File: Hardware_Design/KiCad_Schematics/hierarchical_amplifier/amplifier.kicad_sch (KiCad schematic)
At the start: 8 parts, among them Q1 BC547

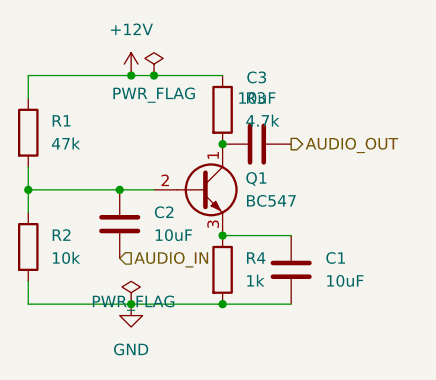
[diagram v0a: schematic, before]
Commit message: Add README for Hierarchical Amplifier circuit
Added the README.md file for the Hierarchical Amplifier project. This file includes the project purpose, component details, functional explanation of the circuit elements (voltage divider, coupling/bypass capacitors), and schematic references to support the hierarchical design documentation.
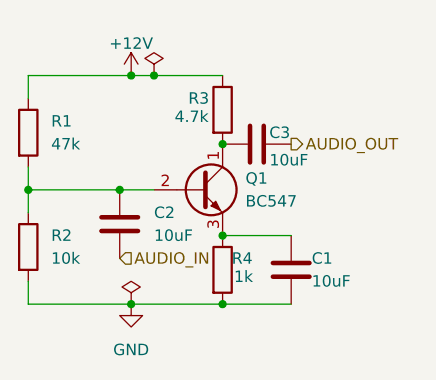
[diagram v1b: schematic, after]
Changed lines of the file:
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@@
 		)
 		(instances
-			(project "kurs4"
+			(project "hierarchical_amplifier"
 				(path "/1680d475-8d12-44de-9d5b-0889d33728e7/cbe5c0ee-a82d-4d0f-91ce-87dab7d0ab98"
 					(reference "#PWR03")
@@
 		(in_pos_files yes)
 		(dnp no)
-		(fields_autoplaced yes)
 		(property "Reference" "#PWR01"
 			(at 133.35 90.17 0)
@@
 		)
 		(property "Value" "+12V"
-			(at 133.35 81.28 0)
+			(at 133.35 82.804 0)
 			(show_name no)
 			(do_not_autoplace no)
@@
 		)
 		(instances
-			(project "kurs4"
+			(project "hierarchical_amplifier"
 				(path "/1680d475-8d12-44de-9d5b-0889d33728e7/cbe5c0ee-a82d-4d0f-91ce-87dab7d0ab98"
 					(reference "#PWR01")
@@
 		)
 		(instances
-			(project "kurs4"
+			(project "hierarchical_amplifier"
 				(path "/1680d475-8d12-44de-9d5b-0889d33728e7/cbe5c0ee-a82d-4d0f-91ce-87dab7d0ab98"
 					(reference "Q1")
@@
 		)
 		(instances
-			(project "kurs4"
+			(project "hierarchical_amplifier"
 				(path "/1680d475-8d12-44de-9d5b-0889d33728e7/cbe5c0ee-a82d-4d0f-91ce-87dab7d0ab98"
 					(reference "R1")
@@
 		)
 		(property "Value" "PWR_FLAG"
-			(at 135.89 88.392 0)
+			(at 134.366 88.138 0)
+			(hide yes)
 			(show_name no)
 			(do_not_autoplace no)
@@
 		)
 		(instances
-			(project "kurs4"
+			(project "hierarchical_amplifier"
 				(path "/1680d475-8d12-44de-9d5b-0889d33728e7/cbe5c0ee-a82d-4d0f-91ce-87dab7d0ab98"
 					(reference "#FLG01")
@@
 		(property "Value" "PWR_FLAG"
 			(at 133.604 111.506 0)
+			(hide yes)
 			(show_name no)
 			(do_not_autoplace no)
@@
 		)
 		(instances
-			(project "kurs4"
+			(project "hierarchical_amplifier"
 				(path "/1680d475-8d12-44de-9d5b-0889d33728e7/cbe5c0ee-a82d-4d0f-91ce-87dab7d0ab98"
 					(reference "#FLG02")
@@
 		(in_pos_files yes)
 		(dnp no)
-		(fields_autoplaced yes)
 		(property "Reference" "R4"
-			(at 146.05 106.6799 0)
+			(at 144.526 106.68 0)
 			(show_name no)
 			(do_not_autoplace no)
@@
 		)
 		(property "Value" "1k"
-			(at 146.05 109.2199 0)
+			(at 144.78 108.712 0)
 			(show_name no)
 			(do_not_autoplace no)
@@
 		)
 		(instances
-			(project "kurs4"
+			(project "hierarchical_amplifier"
 				(path "/1680d475-8d12-44de-9d5b-0889d33728e7/cbe5c0ee-a82d-4d0f-91ce-87dab7d0ab98"
 					(reference "R4")
@@
 		(dnp no)
 		(property "Reference" "C3"
-			(at 147.32 86.614 90)
+			(at 149.86 92.71 90)
 			(show_name no)
 			(do_not_autoplace no)
@@
 		)
 		(property "Value" "10uF"
-			(at 147.32 88.9 90)
+			(at 150.876 95.758 90)
 			(show_name no)
 			(do_not_autoplace no)
@@
 		)
 		(instances
-			(project "kurs4"
+			(project "hierarchical_amplifier"
 				(path "/1680d475-8d12-44de-9d5b-0889d33728e7/cbe5c0ee-a82d-4d0f-91ce-87dab7d0ab98"
 					(reference "C3")
@@
 		)
 		(instances
-			(project "kurs4"
+			(project "hierarchical_amplifier"
 				(path "/1680d475-8d12-44de-9d5b-0889d33728e7/cbe5c0ee-a82d-4d0f-91ce-87dab7d0ab98"
 					(reference "C2")
@@
 		(in_pos_files yes)
 		(dnp no)
-		(fields_autoplaced yes)
 		(property "Reference" "R3"
-			(at 146.05 88.8999 0)
+			(at 139.7 88.9 0)
 			(show_name no)
 			(do_not_autoplace no)
@@
 		)
 		(property "Value" "4.7k"
-			(at 146.05 91.4399 0)
+			(at 138.176 90.932 0)
 			(show_name no)
 			(do_not_autoplace no)
@@
 		)
 		(instances
-			(project "kurs4"
+			(project "hierarchical_amplifier"
 				(path "/1680d475-8d12-44de-9d5b-0889d33728e7/cbe5c0ee-a82d-4d0f-91ce-87dab7d0ab98"
 					(reference "R3")
@@
 		)
 		(instances
-			(project "kurs4"
+			(project "hierarchical_amplifier"
 				(path "/1680d475-8d12-44de-9d5b-0889d33728e7/cbe5c0ee-a82d-4d0f-91ce-87dab7d0ab98"
 					(reference "R2")
@@
 		(in_pos_files yes)
 		(dnp no)
-		(fields_autoplaced yes)
 		(property "Reference" "C1"
-			(at 154.94 106.6799 0)
+			(at 153.416 106.68 0)
 			(show_name no)
 			(do_not_autoplace no)
@@
 		)
 		(property "Value" "10uF"
-			(at 154.94 109.2199 0)
+			(at 153.416 109.22 0)
 			(show_name no)
 			(do_not_autoplace no)
@@
 		)
 		(instances
-			(project "kurs4"
+			(project "hierarchical_amplifier"
 				(path "/1680d475-8d12-44de-9d5b-0889d33728e7/cbe5c0ee-a82d-4d0f-91ce-87dab7d0ab98"
 					(reference "C1")

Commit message: feat(hierarchical_amplifier): add info to Symbols Fields Table
Populated MPN, Manufacturer, and LCSC fields in the Symbol Fields Table
to practice using the Bulk Edit Symbol Fields tool in KiCad.
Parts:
- C1, C2, C3: LCSC (none) -> C576517; Manufacturer (none) -> Murata Electronics; Manufacturer Part Number (none) -> GRM32EC72A106KE05L
- Q1: LCSC (none) -> C47089404; Manufacturer (none) -> onsemi; Manufacturer Part Number (none) -> BC547
- R1: LCSC (none) -> C126351; Manufacturer (none) -> YAGEO; Manufacturer Part Number (none) -> RC0805FR-0747KL
- R2: LCSC (none) -> C84376; Manufacturer (none) -> YAGEO; Manufacturer Part Number (none) -> RC0805FR-0710KL
- R3: LCSC (none) -> C60816; Manufacturer (none) -> YAGEO; Manufacturer Part Number (none) -> RC0805FR-074K7L
- R4: LCSC (none) -> C95781; Manufacturer (none) -> YAGEO; Manufacturer Part Number (none) -> RC0805FR-071KL
